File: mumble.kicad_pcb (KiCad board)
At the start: 2 copper layers, 100 x 30 mm, 65 parts, among them J1 Serial, J101 USB_B_Micro, J11 X_MOT, J16 Z_MOT, J2 Servo, J3 VM sel, Q1 IRLML9301, Q2 IRLML9301, SW1 SW_SPST, SW2 Reset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

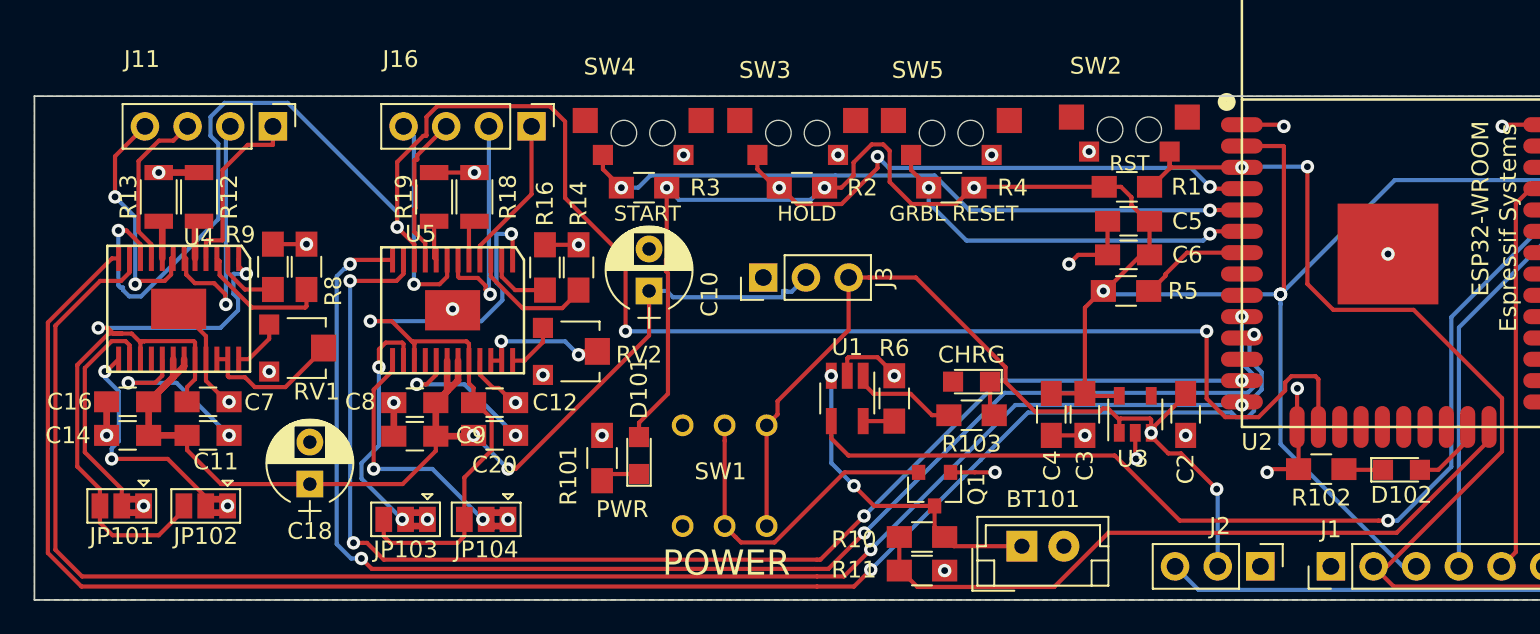
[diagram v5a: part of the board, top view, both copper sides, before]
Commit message: version 1.3, fixed nsleep, chrg led not working. change motor pinout for neater routing.
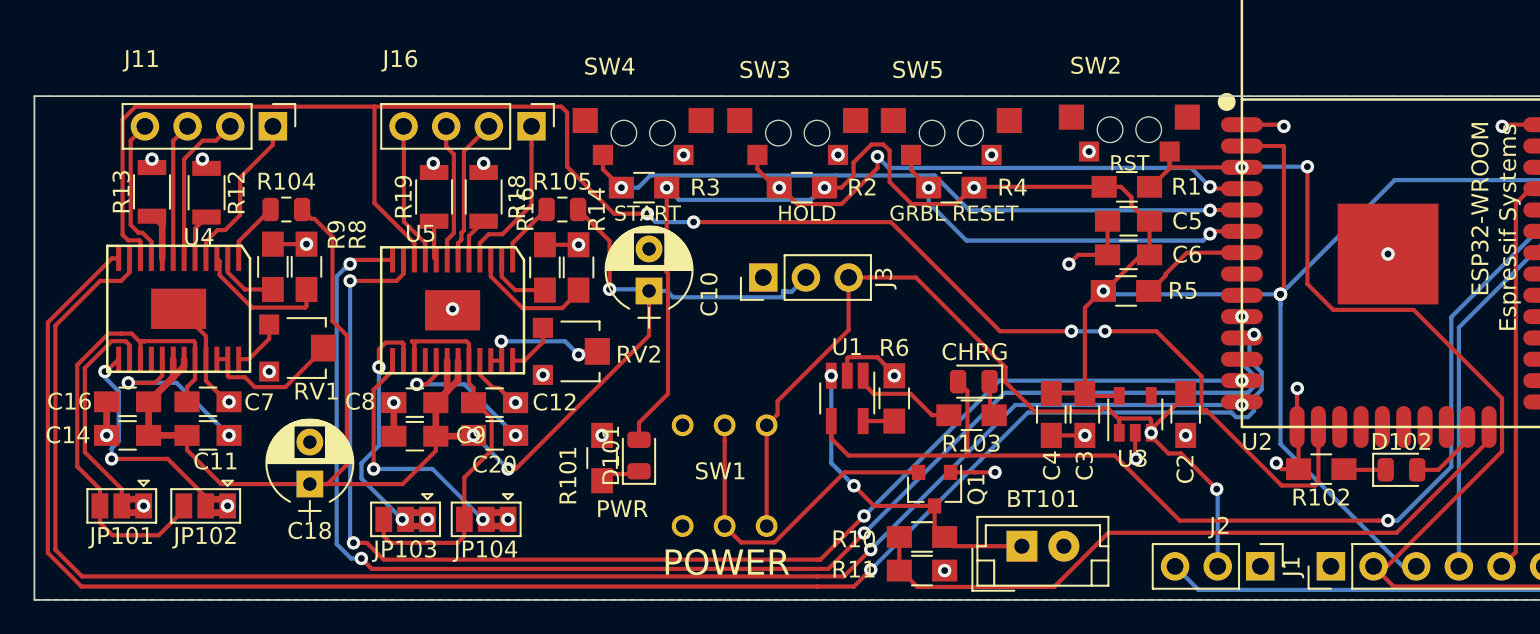
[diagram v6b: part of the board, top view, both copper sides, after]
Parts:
- removed CHRG: CHRG, LEDs:LED_0805
- added D103: CHRG, LED_SMD:LED_0805_2012Metric, F.Cu at (140.9, 152.0)
- added R104: 47k, Resistor_SMD:R_0805_2012Metric, F.Cu at (100.0, 141.8)
- added R105: 47k, Resistor_SMD:R_0805_2012Metric, F.Cu at (116.4, 141.8)
- D101, D102: footprint LEDs:LED_0805 -> LED_SMD:LED_0805_2012Metric
- J1: footprint Pin_Headers:Pin_Header_Straight_1x06_Pitch2.54mm -> Connector_PinHeader_2.54mm:PinHeader_1x06_P2.54mm_Vertical
- moved R18 0.55 mm to (111.8, 141.0)
- moved R12 0.51 mm to (95.2, 140.8)
- moved R13 0.50 mm to (92.0, 140.7)
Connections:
- net Net-(Q2-Pad2) renamed /BATT_PROT
- U4 pad 1: /VINT_X -> Net-(R104-Pad1)
- U4 pad 7: Net-(J11-Pad4) -> Net-(J11-Pad3)
- U4 pad 9: Net-(J11-Pad3) -> Net-(J11-Pad4)
- U5 pad 1: /VINT_Y -> Net-(R105-Pad1)
- U5 pad 7: Net-(J16-Pad4) -> Net-(J16-Pad3)
- U5 pad 9: Net-(J16-Pad3) -> Net-(J16-Pad4)
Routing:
- net /VM: track 66.6 -> 93.6 mm, vias 2 -> 3
- net /VINT_Y: track 41.5 -> 23.6 mm, vias 2 -> 0
- net /VINT_X: track 43.4 -> 28.9 mm, vias 2 -> 0
- net /STEP_EN: track 117.9 -> 106.8 mm
- net Net-(J11-Pad2): track 15.4 -> 9.66 mm, vias 1 -> 0
- net Net-(J11-Pad4): track 14.1 -> 8.86 mm, vias 2 -> 0
- net Net-(J16-Pad2): track 13.5 -> 8.71 mm, vias 1 -> 0
- net /BATT_PROT: track 75.4 -> 80.0 mm
- net Net-(J16-Pad4): track 12.8 -> 8.49 mm, vias 1 -> 0
- net Net-(R105-Pad1): track 0.00 -> 3.85 mm
- net Net-(R104-Pad1): track 0.00 -> 3.70 mm
- net GND: track 57.8 -> 54.8 mm, vias 35 -> 37
- net Net-(J11-Pad1): track 11.7 -> 9.78 mm
- net Net-(J11-Pad3): track 9.89 -> 8.22 mm
- net Net-(J16-Pad3): track 9.12 -> 8.30 mm
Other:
- board text added: "CHRG"
- board text added: "MINIGRAPH V1.3"
- board text removed: "MINIGRAPH V1.0"
